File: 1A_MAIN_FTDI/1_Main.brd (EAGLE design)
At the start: 67.4 x 54.8 mm, 43 parts, among them IC1 NCP1117-33ST, IC10 FT232RL, IC2 MCP1700T-1802E, IC7 MAX14932, IC8 MAX14932, IC9 MAX14932, Q1 IRF7416, X14 ALLSERIALMM, X2 MINI-USB-32005-201, X3 AKL18X-04W

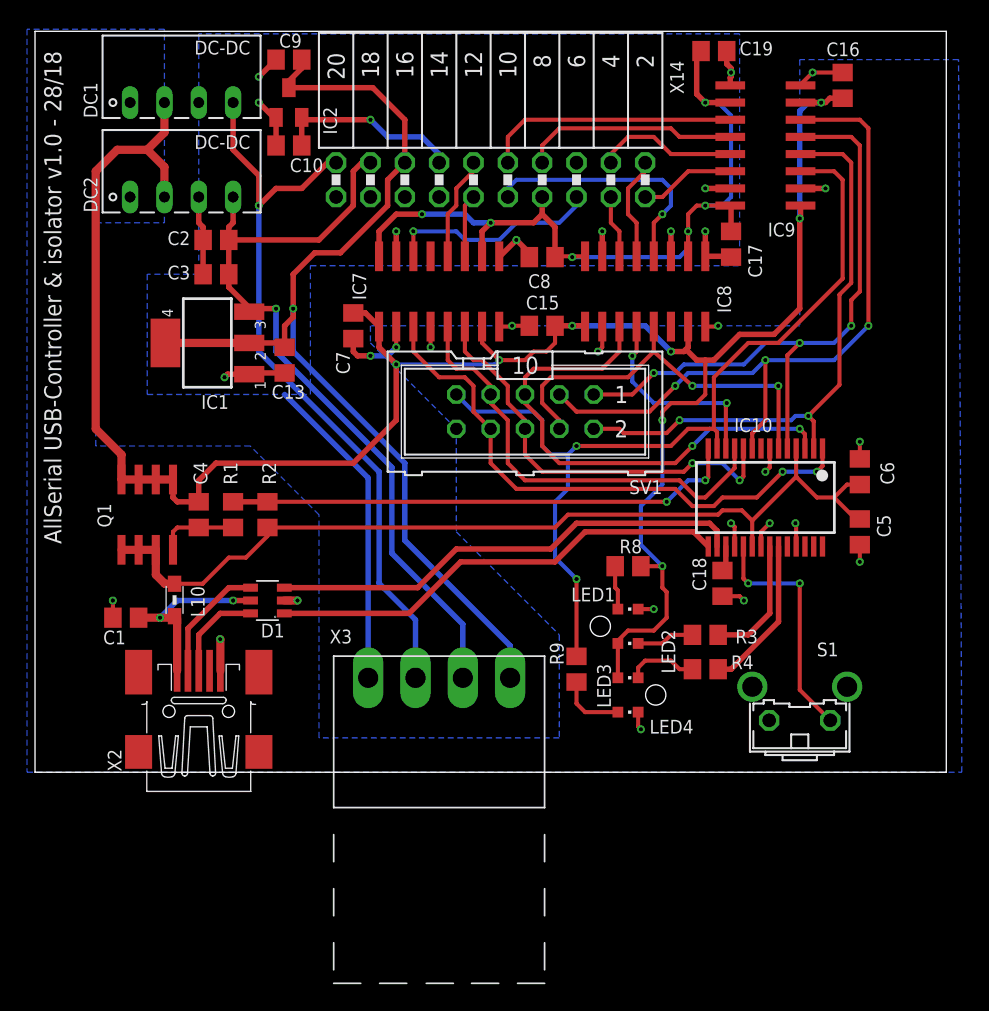
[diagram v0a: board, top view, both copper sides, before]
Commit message: new lib, change pinout!
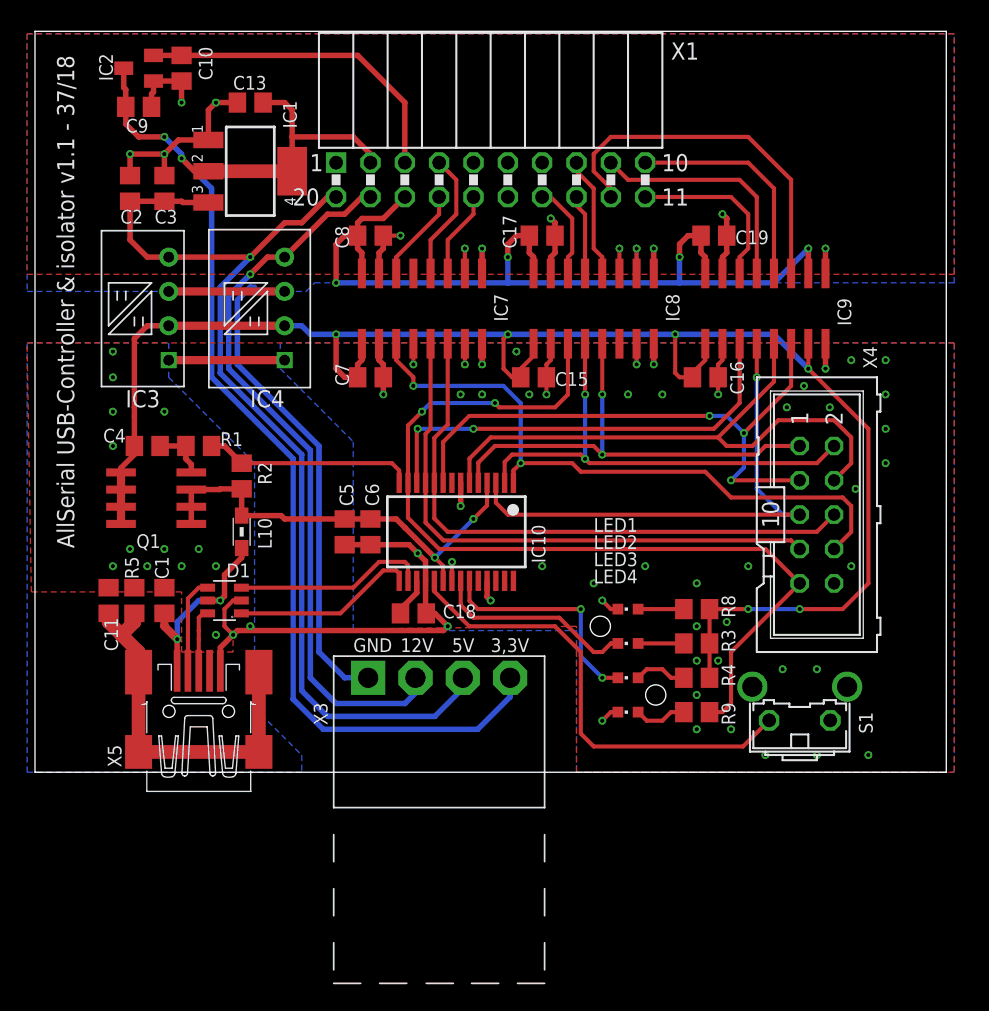
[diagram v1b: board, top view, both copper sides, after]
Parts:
- removed DC1: IL0512S, dc-dc-converter:NME
- removed DC2: CRE1S0505S3C, dc-dc-converter:NME
- removed SV1: (no value), con-harting-ml:ML10
- removed X14: ALLSERIALMM, AllSerial:MAIN-THT
- added C11: 10n, rcl:C0805
- added IC3: CRE1S0505SC, dc-dc-converter:MURATA-SC
- added IC4: IL0512SS, dc-dc-converter:XPPOWER-SIP
- added R5: 1M, rcl:R0805
- added X1: ALLSERIALMASTERMM, AllSerialv2:MAIN-THT
- added X4: (no value), con-harting-ml:ML10
- R8, R9: value 180 -> 270
- X5: value MINI-USB-32005-201 -> MINI-USB-SCHIELD-32005-201
- moved C5 38.1 mm to (-10.8, 17.8)
- moved C6 36.5 mm to (-8.89, 17.8), turned to 270 degrees
- moved C16 23.9 mm to (15.9, 29.2), turned to 0 degrees
- moved IC10 23.0 mm to (-2.54, 17.8)
- moved C18 23.0 mm to (-5.71, 11.7), turned to 0 degrees
- moved C13 19.2 mm to (-17.8, 49.5), turned to 180 degrees
- moved C17 14.0 mm to (3.81, 39.7), turned to 0 degrees
- moved C19 13.7 mm to (16.5, 39.7)
- moved IC1 13.1 mm to (-17.8, 44.5), turned to 270 degrees
- moved C8 12.8 mm to (-8.89, 39.7), turned to 0 degrees
- moved IC9 12.1 mm to (20.3, 34.3), turned to 0 degrees
- moved C9 11.6 mm to (-26.0, 49.2), turned to 0 degrees
- moved IC2 11.4 mm to (-26.0, 52.1), turned to 90 degrees
- moved C10 9.78 mm to (-22.9, 52.1), turned to 270 degrees
- moved R9 9.44 mm to (15.2, 4.45), turned to 0 degrees
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- renumbered X2 to X5
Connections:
- new net N$16: C11.1, R5.1, X5.M1, X5.M2, X5.M3, X5.M4
- net +12V/1: now also IC4.4, X1.19; no longer DC1.4, X14.20
- net +1V8/1: now also X1.3; no longer X14.14
- net +3V3/1: now also X1.2; no longer X14.16
- net +5V: now also IC3.2, IC4.2, R3.1, R4.1; no longer DC1.2, DC2.2, LED2.A, LED3.A
- net +5V/1: now also IC3.4, X1.20; no longer DC2.4, X14.18
- net GND: now also C11.2, IC3.1, IC4.1, R5.2, S1.2, X4.10; no longer DC1.1, DC2.1, S1.1, SV1.10
- net GND1: now also IC3.3, IC4.3, X1.1; no longer DC1.3, DC2.3, X14.19
- net N$1: now also IC8.5, X4.1; no longer IC9.5, SV1.1
- net N$13: now also IC9.3; no longer IC8.4
- net N$14: now also X4.8; no longer SV1.8
- net N$2: now also X4.3; no longer SV1.3
- net N$29: now also IC9.4, X4.5; no longer IC8.3, SV1.5
- net N$3: now also IC8.3, X4.9; no longer IC9.3, SV1.9
- net N$32: now also X4.7; no longer SV1.7
- net N$33: now also IC8.4, X4.2; no longer IC9.4, SV1.2
- net N$35: now also X4.6; no longer SV1.6
- net N$36: now also IC9.5, X4.4; no longer IC8.5, SV1.4
- net N$4: now also LED2.A, R3.2; no longer LED3.C, R4.1
- net N$5: now also S1.1; no longer S1.2
- net N$6: now also LED3.A, R4.2; no longer LED2.C, R3.1
- net N$80: now also X1.17; no longer X14.5
- net N$81: now also IC8.12, X1.8; no longer IC9.12, X14.8
- net N$82: now also IC9.13, X1.9; no longer IC8.14, X14.3
- net N$83: now also X1.4; no longer X14.12
- net N$84: now also IC8.13, X1.13; no longer IC9.13, X14.4
- net N$85: now also X1.12; no longer X14.10
- net N$86: now also X1.16; no longer X14.11
- net N$87: now also IC9.12, X1.10; no longer IC8.12, X14.9
- net N$88: now also IC8.14, X1.14; no longer IC9.14, X14.1
- net N$89: now also IC9.14, X1.11; no longer IC8.13, X14.2
- net RXLED: now also LED2.C; no longer R3.2
- net TXLED: now also LED3.C; no longer R4.2
- net VIN1: now also X1.18; no longer X14.7
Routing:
- net N$38: track 68.6 -> 32.9 mm, vias 0 -> 2
- net GND: track 37.0 -> 69.4 mm, vias 20 -> 62
- net +5V: track 163.7 -> 131.6 mm
- net N$16: track 0.00 -> 28.0 mm
- net GND1: track 56.9 -> 83.8 mm, vias 10 -> 11
- net !PWEN: track 38.0 -> 15.5 mm, vias 2 -> 0
- net N$9: track 35.4 -> 14.4 mm
- net N$10: track 34.3 -> 13.6 mm
- net +3V3/1: track 76.6 -> 94.8 mm, vias 1 -> 2
- net N$13: track 15.2 -> 33.0 mm
- net +5V/1: track 58.6 -> 76.1 mm
- net N$5: track 17.8 -> 34.6 mm, vias 2 -> 0
- net N$36: track 29.7 -> 44.6 mm, vias 2 -> 0
- net VIN1: track 60.0 -> 74.7 mm
- net N$1: track 47.6 -> 34.5 mm, vias 3 -> 2
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- added copper zone on layer 1, net GND
- added copper zone on layer 1, net GND1
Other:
- board text added: "12V"
- board text added: "3,3V"
- board text added: "5V"
- board text added: "AllSerial USB-Controller & isolator v1.1 - 37/18"
- board text added: "GND"
- board text removed: "AllSerial USB-Controller & isolator v1.0 - 28/18"

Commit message: final design & order
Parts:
- moved C4 0.64 mm to (-26.0, 24.1)
- moved L10 0.64 mm to (-19.1, 17.8)
- moved R1 0.64 mm to (-22.2, 24.1)
- moved R2 0.64 mm to (-19.1, 21.9)
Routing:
- net N$14: track 47.7 -> 48.8 mm
- net !PWEN: track 15.5 -> 16.2 mm
- net GND: vias 62 -> 66
